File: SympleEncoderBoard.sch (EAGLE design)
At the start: 31 parts, among them IC1 STM32F446RET6

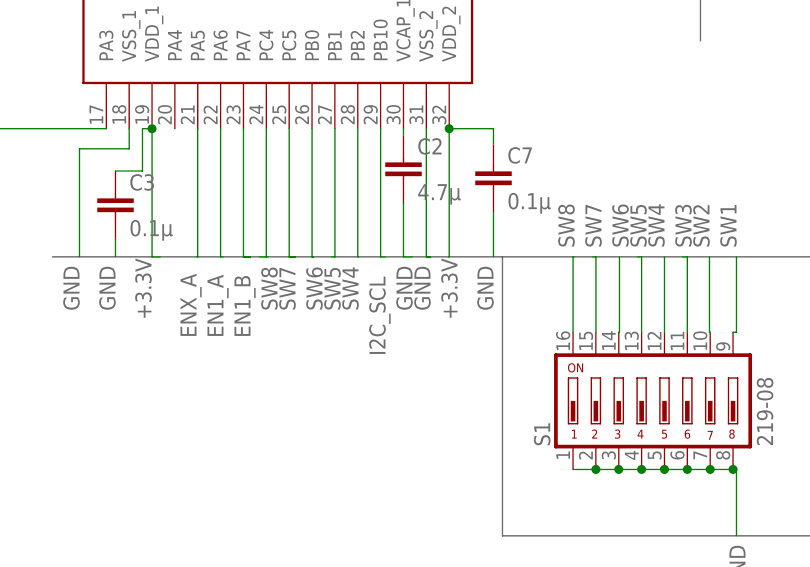
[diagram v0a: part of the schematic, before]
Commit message: 回路図のエラーを直した。部品リストを作成した。
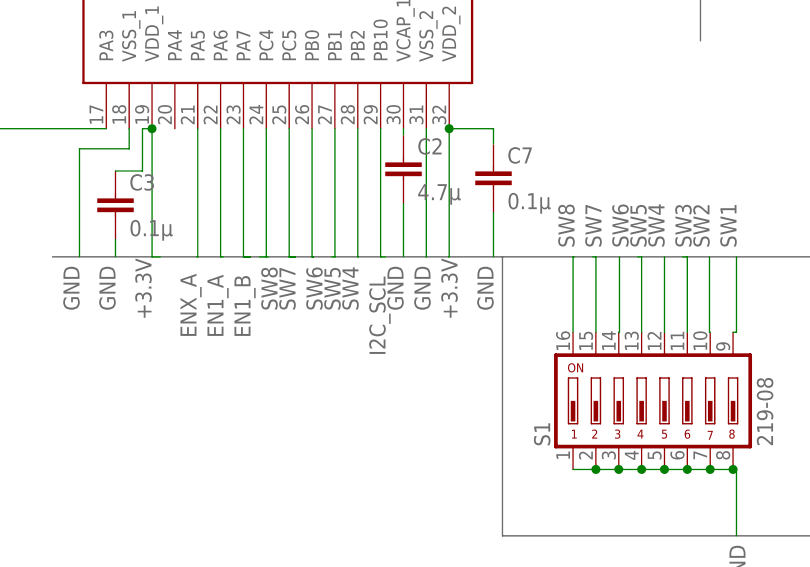
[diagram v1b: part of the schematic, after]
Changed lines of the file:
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@@
 <setting verticaltext="up"/>
 </settings>
-<grid distance="1" unitdist="mm" unit="mm" style="lines" multiple="1" display="yes" altdistance="0.25" altunitdist="mm" altunit="mm"/>
+<grid distance="1" unitdist="mm" unit="mm" style="lines" multiple="1" display="yes" altdistance="0.1" altunitdist="mm" altunit="mm"/>
 <layers>
 <layer number="1" name="Top" color="4" fill="1" visible="no" active="no"/>
@@
 </segment>
 <segment>
-<wire x1="129.54" y1="1" x2="130" y2="1" width="0.1524" layer="91"/>
-</segment>
-<segment>
-<pinref part="IC1" gate="G$1" pin="VSS_2"/>
-<wire x1="129.54" y1="15.24" x2="129.54" y2="1" width="0.1524" layer="91"/>
-<wire x1="129.54" y1="1" x2="130" y2="1" width="0.1524" layer="91"/>
-<label x="130" y="-5" size="1.778" layer="95" rot="R90"/>
-</segment>
-<segment>
-<pinref part="C2" gate="G$1" pin="2"/>
-<wire x1="127" y1="6.92" x2="127" y2="1" width="0.1524" layer="91"/>
-<wire x1="127" y1="1" x2="128" y2="1" width="0.1524" layer="91"/>
-<label x="128" y="-5" size="1.778" layer="95" rot="R90"/>
-</segment>
-<segment>
 <pinref part="C3" gate="G$1" pin="2"/>
 <wire x1="95" y1="2.92" x2="95" y2="1" width="0.1524" layer="91"/>
@@
 <label x="194" y="-51" size="1.778" layer="95"/>
 </segment>
+<segment>
+<pinref part="C2" gate="G$1" pin="2"/>
+<wire x1="127" y1="6.92" x2="127" y2="1" width="0.1524" layer="91"/>
+<label x="127" y="-5" size="1.778" layer="95" rot="R90"/>
+</segment>
+<segment>
+<pinref part="IC1" gate="G$1" pin="VSS_2"/>
+<wire x1="129.54" y1="15.24" x2="129.54" y2="1" width="0.1524" layer="91"/>
+<wire x1="129.54" y1="1" x2="129.5" y2="1" width="0.1524" layer="91"/>
+<label x="130" y="-5" size="1.778" layer="95" rot="R90"/>
+</segment>
 </net>
